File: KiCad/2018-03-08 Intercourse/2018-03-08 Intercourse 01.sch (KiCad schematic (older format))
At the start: 27 parts

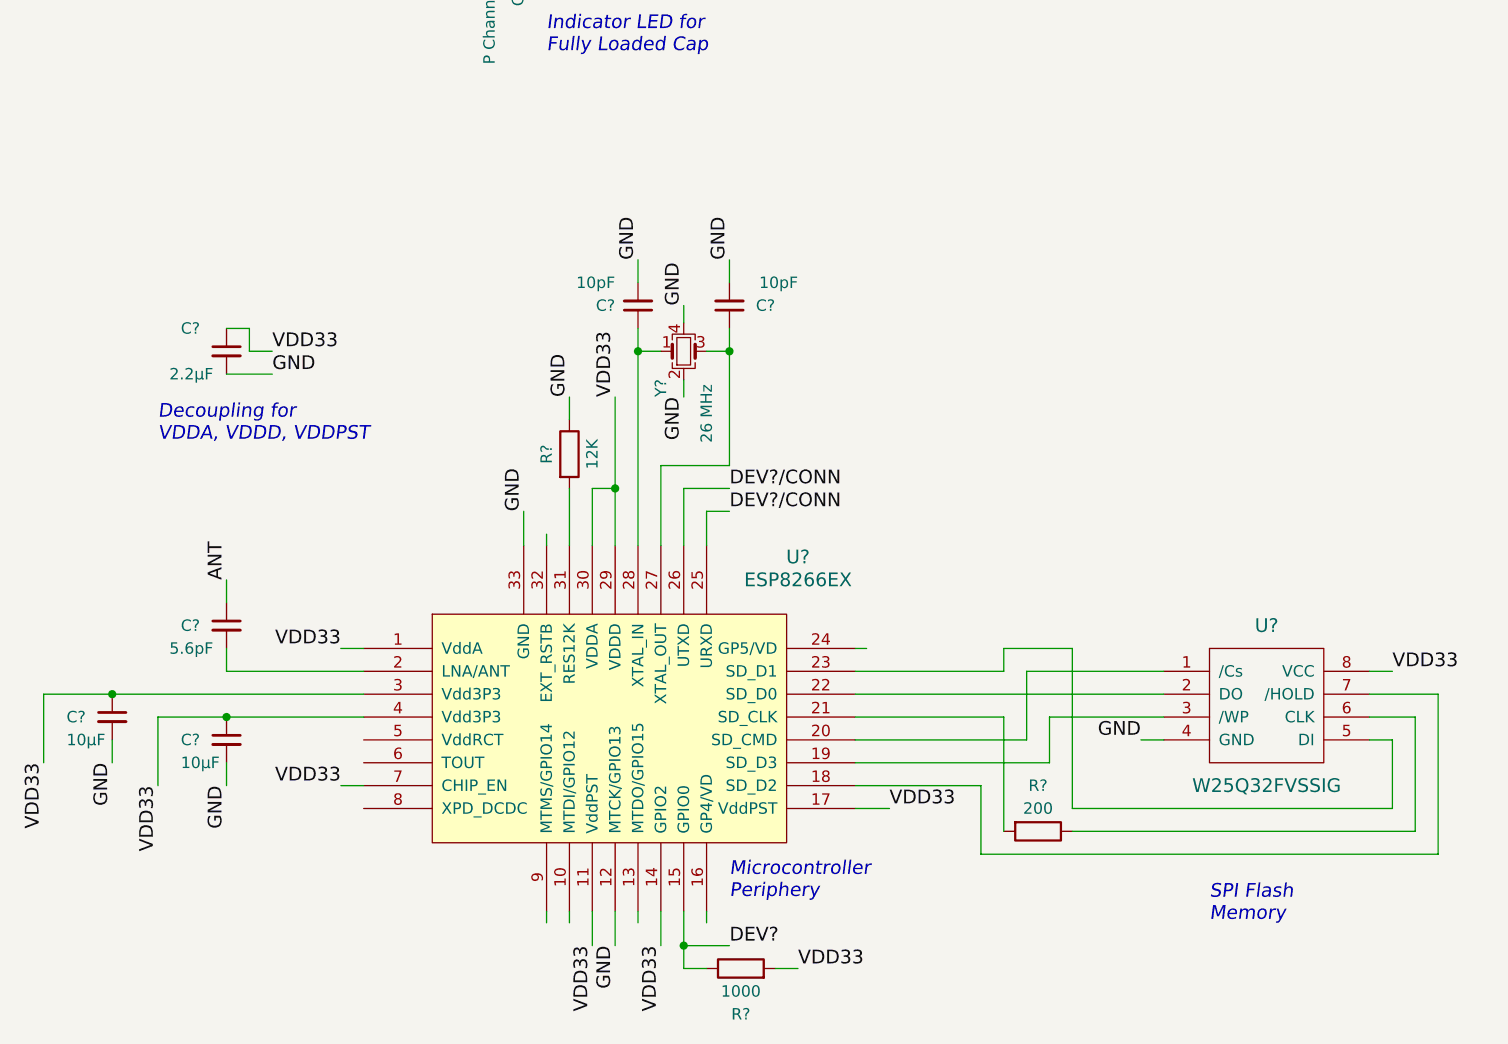
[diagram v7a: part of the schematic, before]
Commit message: schematic edits
* added NCs
* clean up
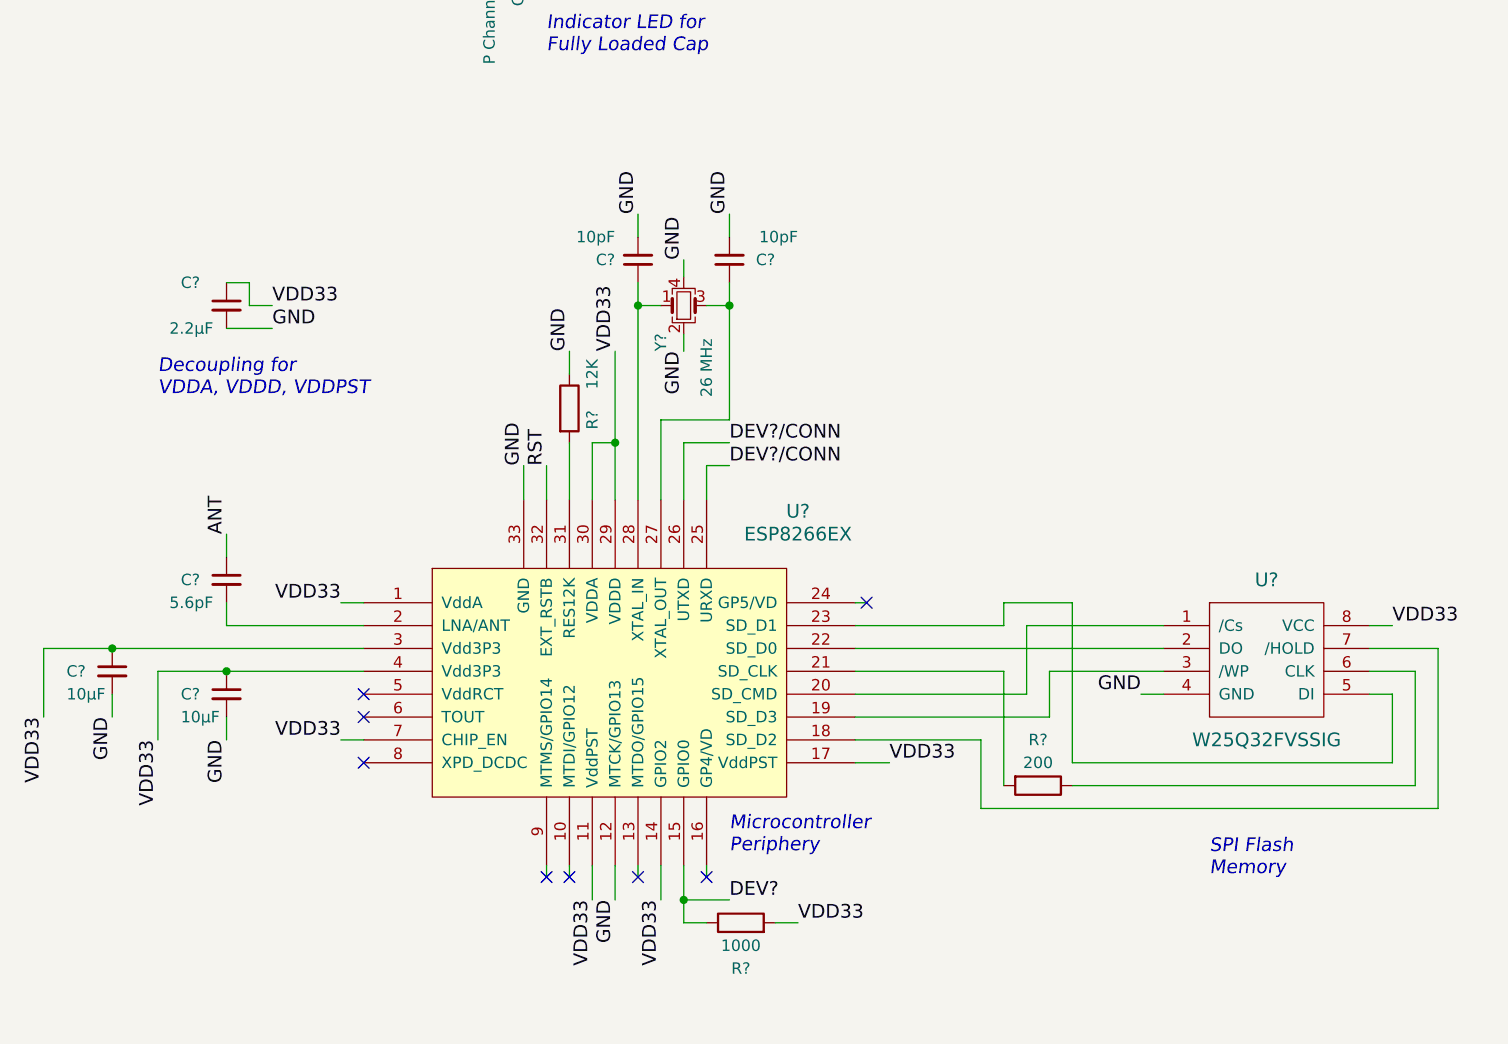
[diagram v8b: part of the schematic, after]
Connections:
- net labels added: RST
- no-connect marks 3 -> 11
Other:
- moved on the sheet: C?, R?, U?, Y?
